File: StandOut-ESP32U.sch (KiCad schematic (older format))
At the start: 12 parts, among them J1 UART_2, J10 Common Pins, J16 Conn_01x18_Male, J2 GPIO, J3 Common Pins, J4 UART_0, J5 GPIO, J6 Common Pins, J7 GPIO, J8 Common Pins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

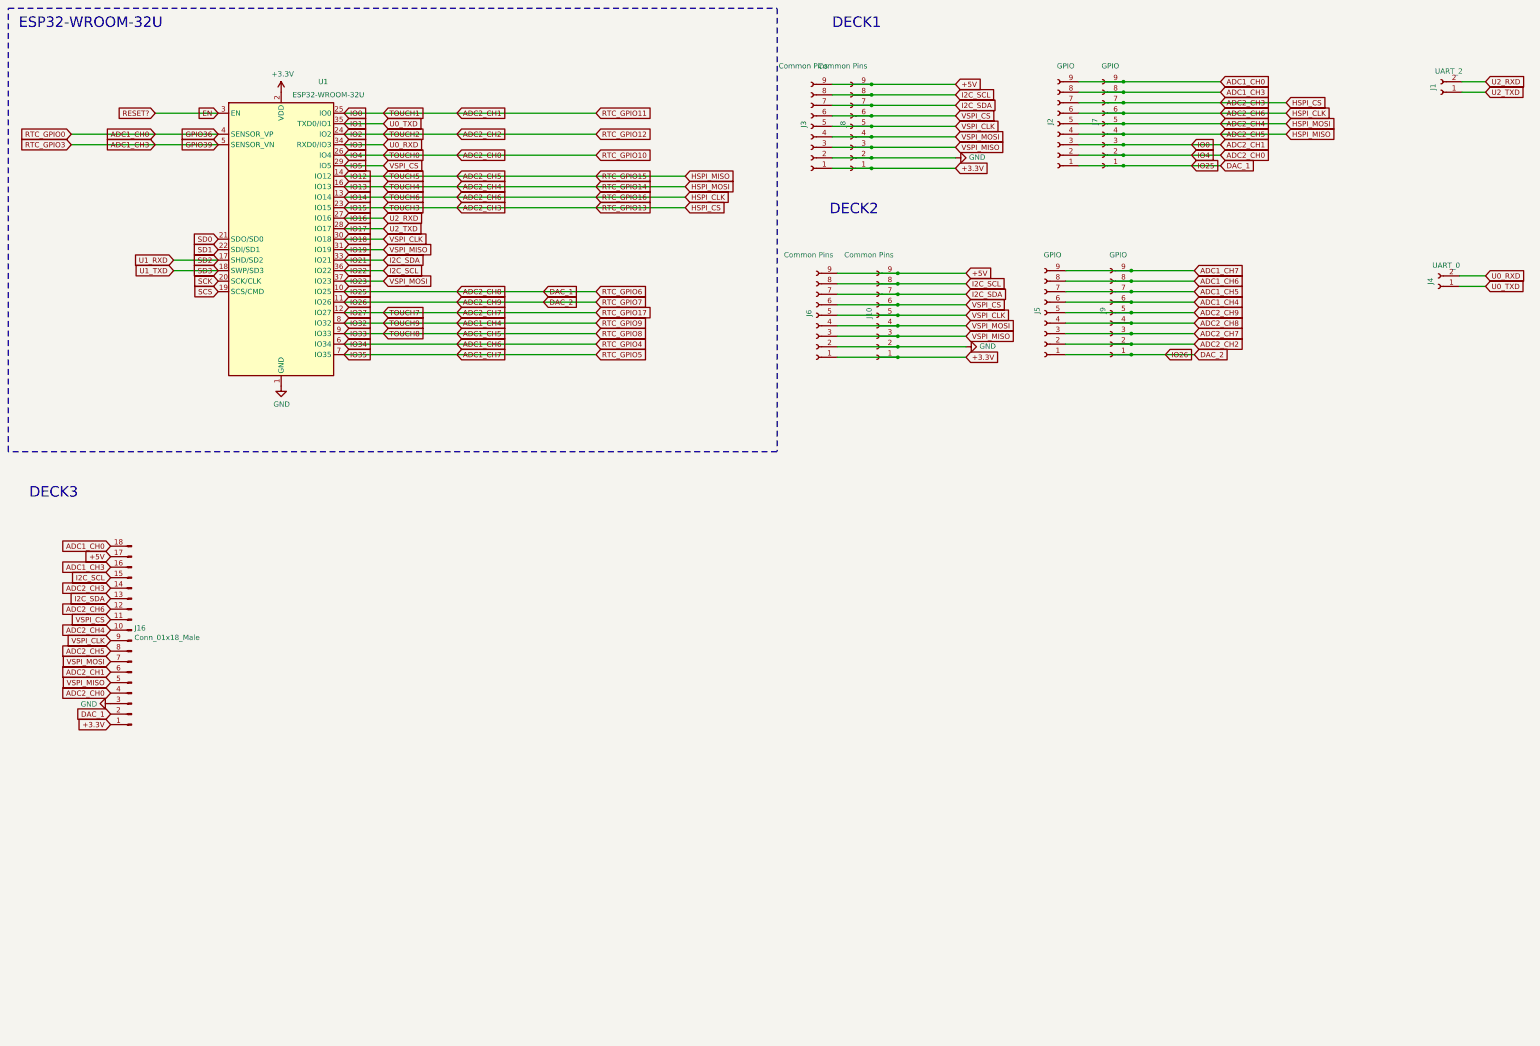
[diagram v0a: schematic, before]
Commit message: Working on Schematic - Micro-USB & UART
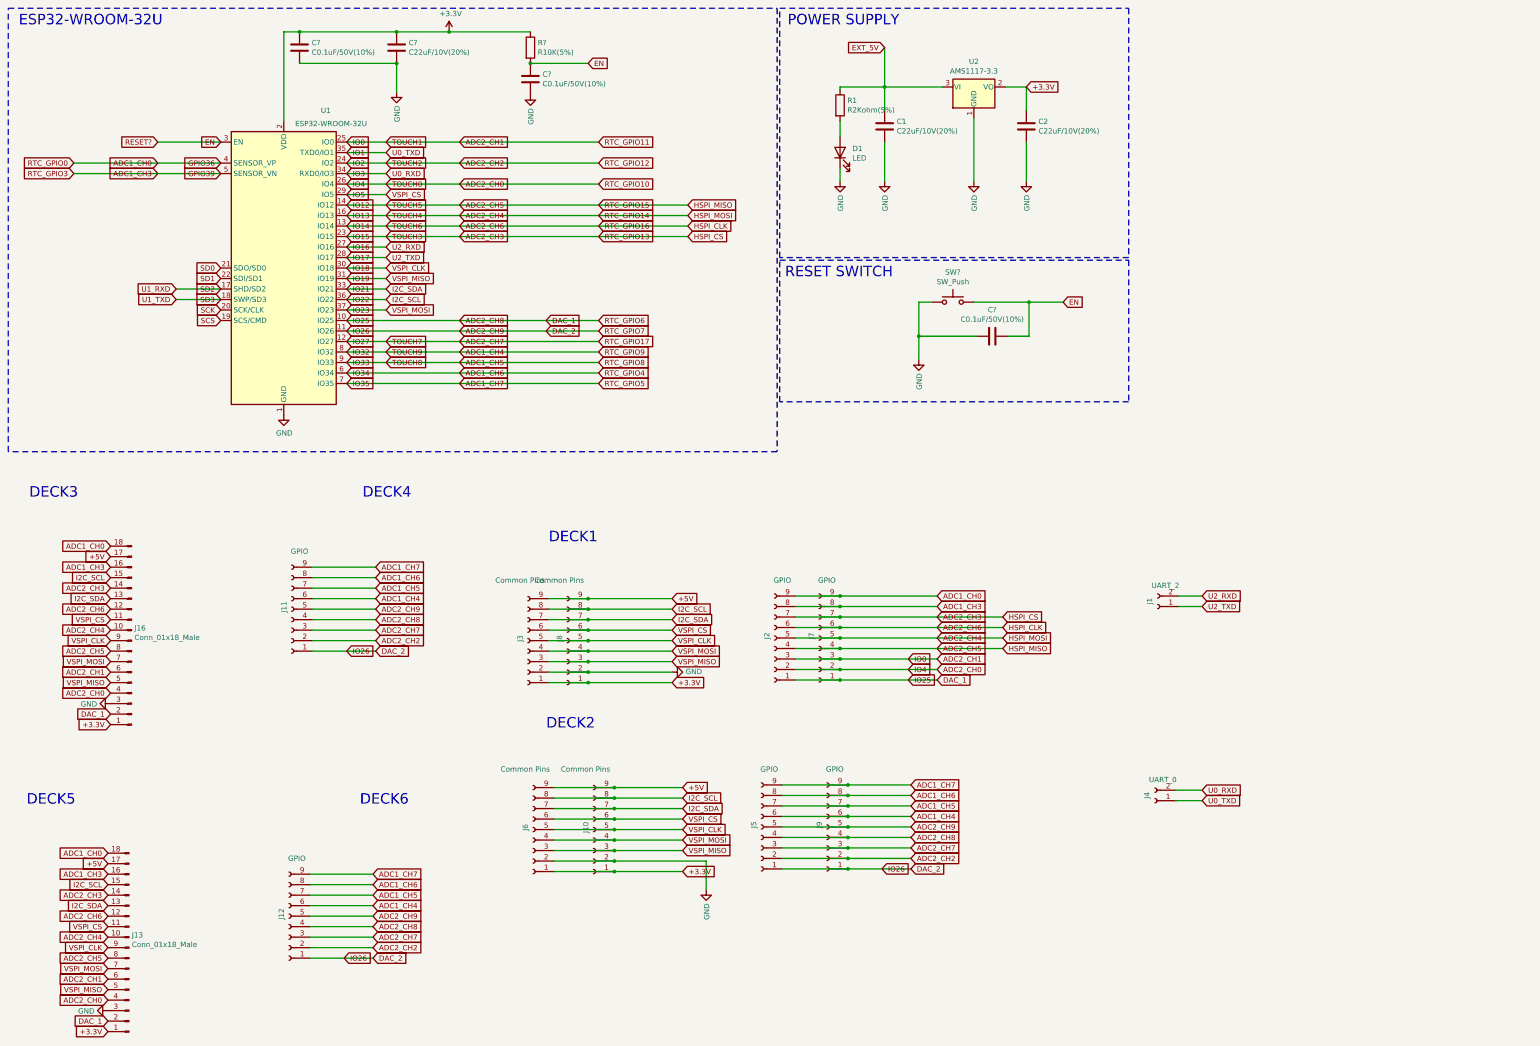
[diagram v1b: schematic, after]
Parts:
- added C1, C2, C?: C22uF/10V(20%), Capacitor_SMD:C_0603_1608Metric, symbol Device:C
- added C? (x3): C0.1uF/50V(10%), Capacitor_SMD:C_0603_1608Metric, symbol Device:C
- added D1: LED, LED_SMD:LED_0805_2012Metric, symbol Device:LED
- added J11: GPIO, Connector_PinSocket_2.54mm:PinSocket_1x09_P2.54mm_Horizontal, symbol Connector:Conn_01x09_Female
- added J12: GPIO, Connector_PinHeader_2.54mm:PinHeader_1x09_P2.54mm_Horizontal, symbol Connector:Conn_01x09_Female
- added J13: Conn_01x18_Male, Connector_PinHeader_2.54mm:PinHeader_2x09_P2.54mm_Horizontal, symbol Connector:Conn_01x18_Male
- added R1: R2Kohm(5%), Resistor_SMD:R_0603_1608Metric, symbol Device:R
- added R?: R10K(5%), Resistor_SMD:R_0402_1005Metric, symbol Device:R
- added SW?: SW_Push, SamacSys_Parts:TL3340, symbol Switch:SW_Push
- added U2: AMS1117-3.3, Package_TO_SOT_SMD:SOT-223-3_TabPin2, symbol Regulator_Linear:AMS1117-3.3
- J16: footprint Connector_PinHeader_2.54mm:PinHeader_2x09_P2.54mm_Horizontal -> Connector_PinSocket_2.54mm:PinSocket_2x09_P2.54mm_Horizontal
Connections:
- net +3.3V: now also C2.1, J13.1 (Pin_1), U2.2 (VO)
- net +3V3: now also C?.1, C?.2, R?.1
- net +5V: now also J13.17 (Pin_17)
- net ADC1_CH0: now also J13.18 (Pin_18)
- net ADC1_CH3: now also J13.16 (Pin_16)
- net ADC1_CH4: now also J11.6 (Pin_6), J12.6 (Pin_6)
- net ADC1_CH5: now also J11.7 (Pin_7), J12.7 (Pin_7)
- net ADC1_CH6: now also J11.8 (Pin_8), J12.8 (Pin_8)
- net ADC1_CH7: now also J11.9 (Pin_9), J12.9 (Pin_9)
- net ADC2_CH0: now also J13.4 (Pin_4)
- net ADC2_CH1: now also J13.6 (Pin_6)
- net ADC2_CH2: now also J11.2 (Pin_2), J12.2 (Pin_2)
- net ADC2_CH3: now also J13.14 (Pin_14)
- net ADC2_CH4: now also J13.10 (Pin_10)
- net ADC2_CH5: now also J13.8 (Pin_8)
- net ADC2_CH6: now also J13.12 (Pin_12)
- net ADC2_CH7: now also J11.3 (Pin_3), J12.3 (Pin_3)
- net ADC2_CH8: now also J11.4 (Pin_4), J12.4 (Pin_4), J13.2 (Pin_2)
- net ADC2_CH9: now also J11.1 (Pin_1), J11.5 (Pin_5), J12.1 (Pin_1), J12.5 (Pin_5)
- net EN: now also C?.2, C?.2, R?.2, SW?.2
- net GND: now also C1.2, C2.2, C?.1, C?.1, C?.1, C?.2, D1.1 (K), J13.3 (Pin_3), SW?.1, U2.1 (GND)
- net I2C_SCL: now also J13.15 (Pin_15)
- net I2C_SDA: now also J13.13 (Pin_13)
- net IO18: now also J13.9 (Pin_9)
- net IO19: now also J13.5 (Pin_5)
- net IO23: now also J13.7 (Pin_7)
- net IO5: now also J13.11 (Pin_11)
- new net: D1.2 (A), R1.2
- new net EXT_5V: C1.1, R1.1, U2.3 (VI)
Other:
- note added: "DECK4"
- note added: "DECK5"
- note added: "DECK6"
- note added: "POWER SUPPLY"
- note added: "RESET SWITCH"
- moved on the sheet: J1, J10, J2, J3, J4, J5, J6, J7, J8, J9, U1
